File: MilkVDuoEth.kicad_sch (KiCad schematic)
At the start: 6 parts, among them J1 Conn_01x05_Female, J2 RJ45-TRANSFORMER_LED_HANRUN

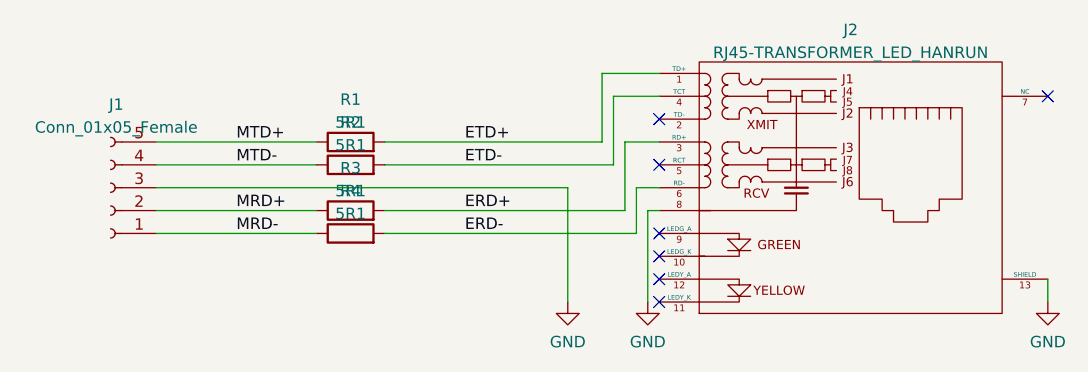
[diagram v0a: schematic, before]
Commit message: Remove all SMT components from PCB.
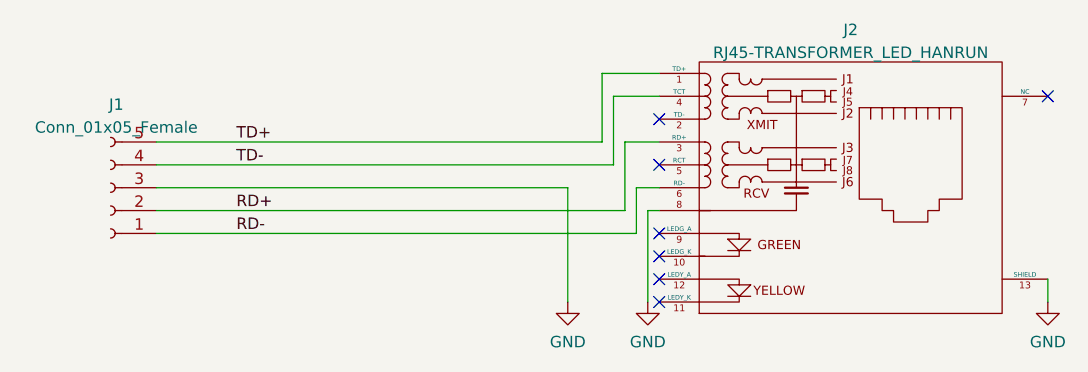
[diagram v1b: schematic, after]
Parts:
- removed R1, R2, R3, R4: 5R1, Resistor_SMD:R_0603_1608Metric_Pad0.98x0.95mm_HandSolder, symbol Device:R
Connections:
- net MRD+ is gone; now on net RD+: J1.2 (Pin_2)
- net MRD- is gone; now on net RD-: J1.1 (Pin_1)
- net MTD+ is gone; now on net TD+: J1.5 (Pin_5)
- net MTD- is gone; now on net TD-: J1.4 (Pin_4)
- net ERD+ renamed RD+
- net ERD- renamed RD-
- net ETD+ renamed TD+
- net ETD- renamed TD-
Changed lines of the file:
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@@
   (title_block
     (title "MilkV-Duo Ethernet")
-    (date "2023-07-25")
-    (rev "0.2")
+    (date "2023-09-15")
+    (rev "0.3")
     (company "Ewan Parker")
   )
@@
     (stroke (width 0) (type default) (color 0 0 0 0))
   )
-  (wire (pts (xy 81.28 104.14) (xy 99.06 104.14))
-    (stroke (width 0) (type default) (color 0 0 0 0))
-  )
   (wire (pts (xy 137.16 101.6) (xy 134.62 101.6))
-    (stroke (width 0) (type default) (color 0 0 0 0))
-  )
-  (wire (pts (xy 106.68 104.14) (xy 133.35 104.14))
     (stroke (width 0) (type default) (color 0 0 0 0))
   )
@@
     (stroke (width 0) (type default) (color 0 0 0 0))
   )
-  (wire (pts (xy 106.68 96.52) (xy 130.81 96.52))
+  (wire (pts (xy 81.28 96.52) (xy 130.81 96.52))
     (stroke (width 0) (type default) (color 0 0 0 0))
   )
@@
     (stroke (width 0) (type default) (color 0 0 0 0))
   )
-  (wire (pts (xy 81.28 99.06) (xy 99.06 99.06))
+  (wire (pts (xy 81.28 106.68) (xy 134.62 106.68))
     (stroke (width 0) (type default) (color 0 0 0 0))
   )
-  (wire (pts (xy 81.28 96.52) (xy 99.06 96.52))
+  (wire (pts (xy 81.28 99.06) (xy 132.08 99.06))
     (stroke (width 0) (type default) (color 0 0 0 0))
   )
@@
     (stroke (width 0) (type default) (color 0 0 0 0))
   )
-  (wire (pts (xy 132.08 99.06) (xy 106.68 99.06))
-    (stroke (width 0) (type default) (color 0 0 0 0))
-  )
   (wire (pts (xy 133.35 104.14) (xy 133.35 96.52))
-    (stroke (width 0) (type default) (color 0 0 0 0))
-  )
-  (wire (pts (xy 134.62 106.68) (xy 106.68 106.68))
     (stroke (width 0) (type default) (color 0 0 0 0))
   )
@@
     (stroke (width 0) (type default) (color 0 0 0 0))
   )
-  (wire (pts (xy 81.28 106.68) (xy 99.06 106.68))
+  (wire (pts (xy 81.28 104.14) (xy 133.35 104.14))
     (stroke (width 0) (type default) (color 0 0 0 0))
   )
@@
     (stroke (width 0) (type default) (color 0 0 0 0))
   )
-  (label "ERD-" (at 115.57 106.68 0)
+  (label "TD+" (at 90.17 96.52 0)
     (effects (font (size 1.27 1.27)) (justify left bottom))
   )
-  (label "ETD+" (at 115.57 96.52 0)
+  (label "RD+" (at 90.17 104.14 0)
     (effects (font (size 1.27 1.27)) (justify left bottom))
   )
-  (label "MTD+" (at 90.17 96.52 0)
+  (label "TD-" (at 90.17 99.06 0)
     (effects (font (size 1.27 1.27)) (justify left bottom))
   )
-  (label "MRD+" (at 90.17 104.14 0)
+  (label "RD-" (at 90.17 106.68 0)
     (effects (font (size 1.27 1.27)) (justify left bottom))
-  )
-  (label "ERD+" (at 115.57 104.14 0)
-    (effects (font (size 1.27 1.27)) (justify left bottom))
-  )
-  (label "MTD-" (at 90.17 99.06 0)
-    (effects (font (size 1.27 1.27)) (justify left bottom))
-  )
-  (label "MRD-" (at 90.17 106.68 0)
-    (effects (font (size 1.27 1.27)) (justify left bottom))
-  )
-  (label "ETD-" (at 115.57 99.06 0)
-    (effects (font (size 1.27 1.27)) (justify left bottom))
-  )
-  (symbol (lib_id "Device:R") (at 102.87 104.14 90) (unit 1)
-    (in_bom yes) (on_board yes) (fields_autoplaced)
-    (property "Reference" "R3" (id 0) (at 102.87 99.4242 90))
-    (property "Value" "5R1" (id 1) (at 102.87 101.9611 90))
-    (property "Footprint" "Resistor_SMD:R_0603_1608Metric_Pad0.98x0.95mm_HandSolder" (id 2) (at 102.87 105.918 90)
-      (effects (font (size 1.27 1.27)) hide)
-    )
-    (property "Datasheet" "~" (id 3) (at 102.87 104.14 0)
-      (effects (font (size 1.27 1.27)) hide)
-    )
-    (pin "1")
-    (pin "2")
-  )
-  (symbol (lib_id "Device:R") (at 102.87 106.68 90) (unit 1)
-    (in_bom yes) (on_board yes) (fields_autoplaced)
-    (property "Reference" "R4" (id 0) (at 102.87 101.9642 90))
-    (property "Value" "5R1" (id 1) (at 102.87 104.5011 90))
-    (property "Footprint" "Resistor_SMD:R_0603_1608Metric_Pad0.98x0.95mm_HandSolder" (id 2) (at 102.87 108.458 90)
-      (effects (font (size 1.27 1.27)) hide)
-    )
-    (property "Datasheet" "~" (id 3) (at 102.87 106.68 0)
-      (effects (font (size 1.27 1.27)) hide)
-    )
-    (pin "1")
-    (pin "2")
   )
   (symbol (lib_id "RJ45:RJ45-TRANSFORMER_LED_HANRUN") (at 165.1 101.6 0) (unit 1)
@@
     (pin "1")
   )
-  (symbol (lib_id "Device:R") (at 102.87 96.52 90) (unit 1)
-    (in_bom yes) (on_board yes) (fields_autoplaced)
-    (property "Reference" "R1" (id 0) (at 102.87 91.8042 90))
-    (property "Value" "5R1" (id 1) (at 102.87 94.3411 90))
-    (property "Footprint" "Resistor_SMD:R_0603_1608Metric_Pad0.98x0.95mm_HandSolder" (id 2) (at 102.87 98.298 90)
-      (effects (font (size 1.27 1.27)) hide)
-    )
-    (property "Datasheet" "~" (id 3) (at 102.87 96.52 0)
-      (effects (font (size 1.27 1.27)) hide)
-    )
-    (pin "1")
-    (pin "2")
-  )
-  (symbol (lib_id "Device:R") (at 102.87 99.06 90) (unit 1)
-    (in_bom yes) (on_board yes) (fields_autoplaced)
-    (property "Reference" "R2" (id 0) (at 102.87 94.3442 90))
-    (property "Value" "5R1" (id 1) (at 102.87 96.8811 90))
-    (property "Footprint" "Resistor_SMD:R_0603_1608Metric_Pad0.98x0.95mm_HandSolder" (id 2) (at 102.87 100.838 90)
-      (effects (font (size 1.27 1.27)) hide)
-    )
-    (property "Datasheet" "~" (id 3) (at 102.87 99.06 0)
-      (effects (font (size 1.27 1.27)) hide)
-    )
-    (pin "1")
-    (pin "2")
-  )
   (sheet_instances
     (path "/" (page "1"))
@@
       (reference "J2") (unit 1) (value "RJ45-TRANSFORMER_LED_HANRUN") (footprint "RJ45:RJ45_HR911105A")
     )
-    (path "/bd2918f2-fc6e-4871-93ff-526f30680bc5"
-      (reference "R1") (unit 1) (value "5R1") (footprint "Resistor_SMD:R_0603_1608Metric_Pad0.98x0.95mm_HandSolder")
-    )
-    (path "/e9a00051-3362-42d5-b6d7-35da0417bf9a"
-      (reference "R2") (unit 1) (value "5R1") (footprint "Resistor_SMD:R_0603_1608Metric_Pad0.98x0.95mm_HandSolder")
-    )
-    (path "/1f5aa310-4907-4069-9fde-5f3bc617abc2"
-      (reference "R3") (unit 1) (value "5R1") (footprint "Resistor_SMD:R_0603_1608Metric_Pad0.98x0.95mm_HandSolder")
-    )
-    (path "/270b8d71-b681-4bbc-bf9d-c3f8ef0d39d2"
-      (reference "R4") (unit 1) (value "5R1") (footprint "Resistor_SMD:R_0603_1608Metric_Pad0.98x0.95mm_HandSolder")
-    )
   )
